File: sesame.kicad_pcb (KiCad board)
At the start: 2 copper layers, 344.4 x 130.9 mm, 164 parts, among them U1 ATmega32A-PU

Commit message: update
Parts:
- added G***: LOGO, custom_parts:qmk, B.Cu at (321.4, 168.5)
- moved G*** 7.82 mm to (336.0, 159.6)
- moved G*** 6.67 mm to (299.3, 168.9)
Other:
- board text added: "Sesame Ergo PCB rev. 1 github.com/kb-elmo/sesame elmo.space"
- board text removed: "Sesame Ergo PCB rev. 1"

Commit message: fix layout and add firmware
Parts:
- MX18: footprint MX_Only:MXOnly-1U-NoLED -> MX_Only:MXOnly-1.5U-NoLED
- MX33: footprint MX_Only:MXOnly-1U-NoLED -> MX_Only:MXOnly-1.75U-NoLED
- MX59: footprint MX_Only:MXOnly-1.5U-NoLED -> MX_Only:MXOnly-1.75U-NoLED
- moved D34 7.75 mm to (97.4, 132.8)
- moved MX33 4.83 mm to (83.8, 127.4)
- moved MX59 2.35 mm to (346.7, 146.5)
- moved D60 1.02 mm to (334.8, 151.6)
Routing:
- net col1: track 214.9 -> 211.0 mm
- net Net-(D34-Pad2): track 9.31 -> 12.2 mm

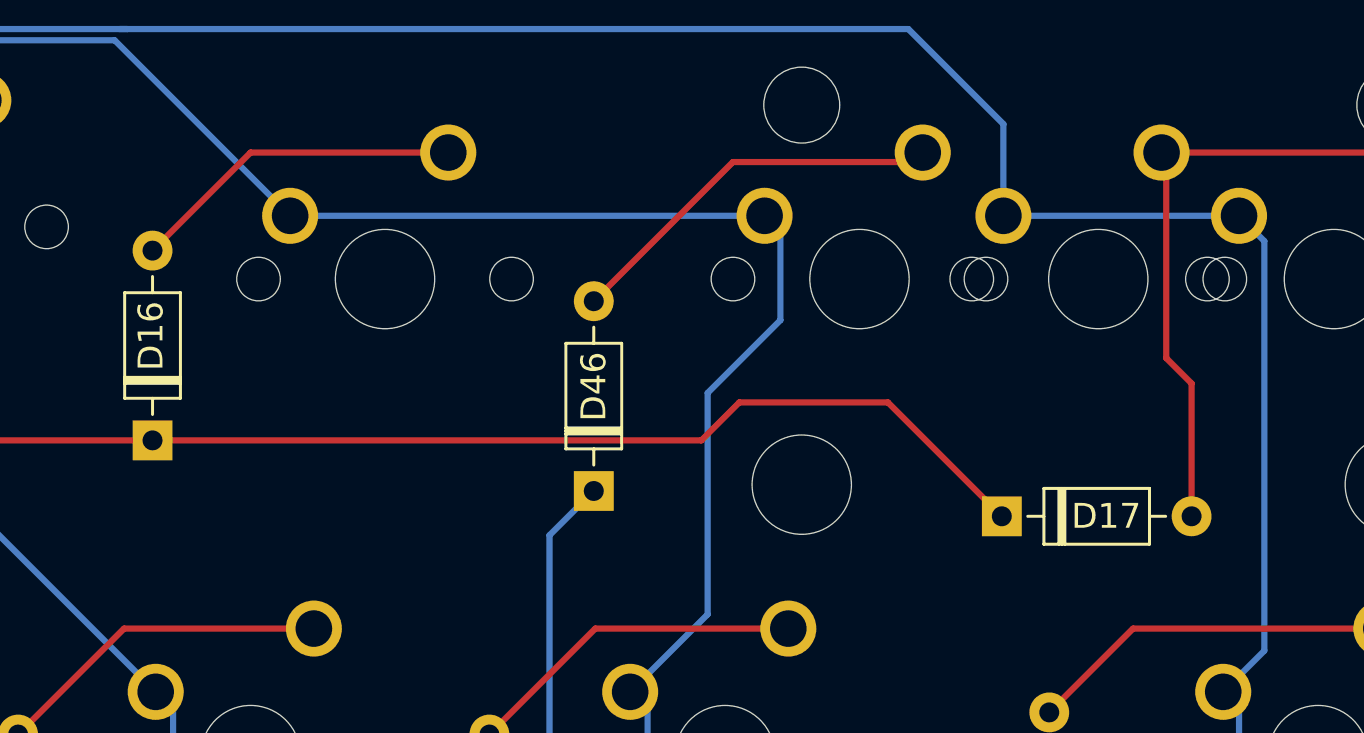
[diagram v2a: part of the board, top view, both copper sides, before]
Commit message: fix diode placement
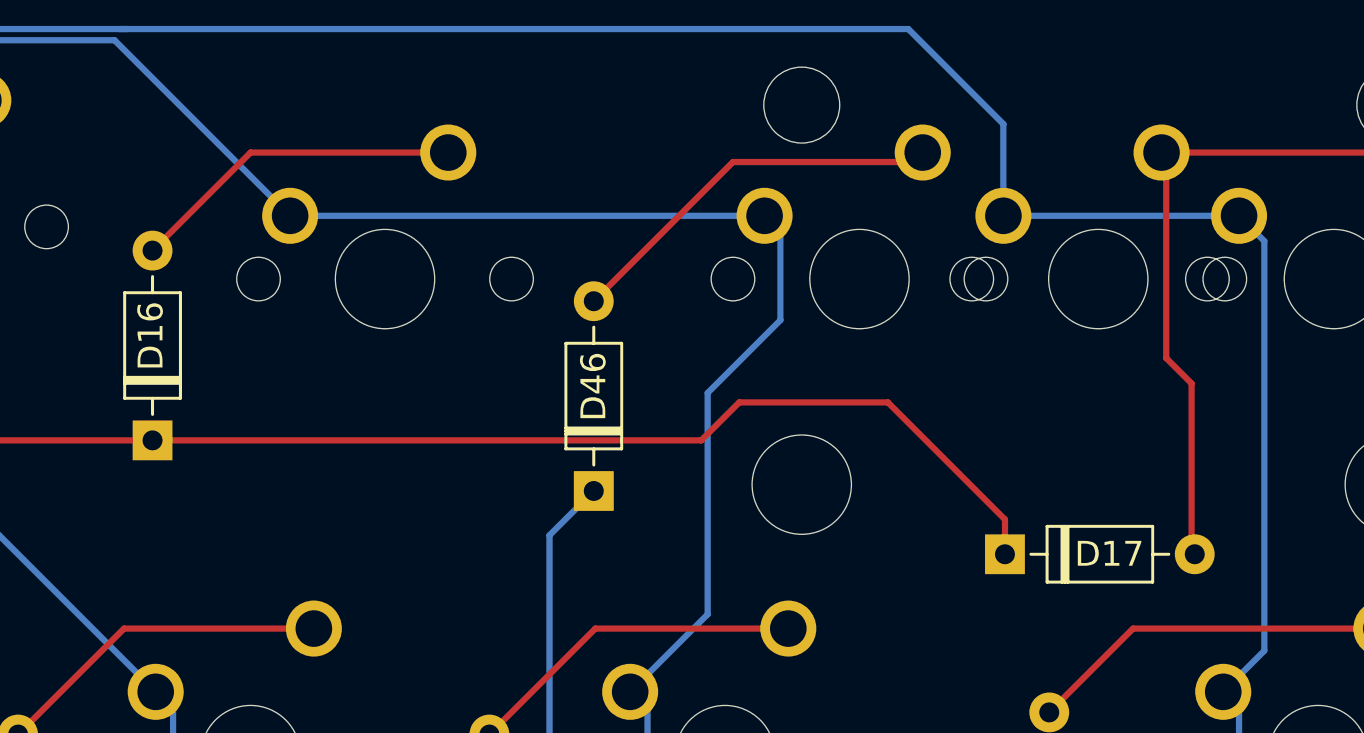
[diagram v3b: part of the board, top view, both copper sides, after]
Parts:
- moved D17 1.53 mm to (347.1, 100.3)
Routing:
- net bs: track 24.6 -> 26.1 mm
- net row0: track 318.4 -> 320.0 mm
